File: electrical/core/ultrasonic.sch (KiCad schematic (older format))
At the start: 7 parts

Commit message: Annotation
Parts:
- gave numbers to parts that had none: 7

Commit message: Updated ultrassonic level shifter
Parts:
- removed Q3, Q4: 2N3904, Package_TO_SOT_THT:TO-92_Inline, symbol Transistor_BJT:2N3904
- removed R73: 2.2k, symbol Device:R
- added Q2, Q3: AO3400, Package_TO_SOT_SMD:SOT-23, symbol rasbot:AO3400
- added R70: 10k, symbol Device:R
- R71: value 2.2k -> 10k
- renumbered J6 to J5, R70 to R68, R72 to R69
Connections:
- net labels added: Power-
- net labels removed: GND
- wire segments 19 -> 20
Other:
- moved on the sheet: R68, R69

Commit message: Several updates. Can't remember them all
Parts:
- R100: renamed from R69; footprint (none) -> Resistor_SMD:R_0603_1608Metric
- R101: renamed from R70; footprint (none) -> Resistor_SMD:R_0603_1608Metric
- R102: renamed from R71; footprint (none) -> Resistor_SMD:R_0603_1608Metric
- R99: renamed from R68; footprint (none) -> Resistor_SMD:R_0603_1608Metric
- renumbered J5 to J10, Q2 to Q6, Q3 to Q7

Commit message: lots of changes
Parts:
- renumbered J10 to J9, R99 to R101, R100 to R102, R101 to R103, R102 to R104

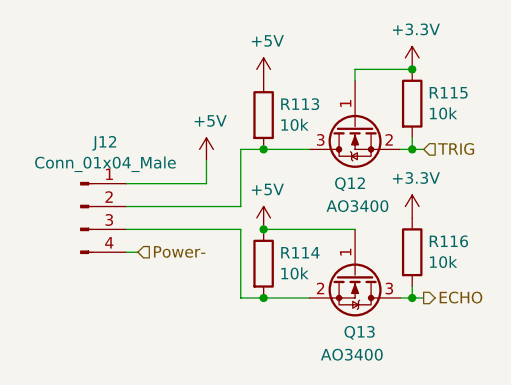
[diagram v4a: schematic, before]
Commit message: Reannotated after LDO romval
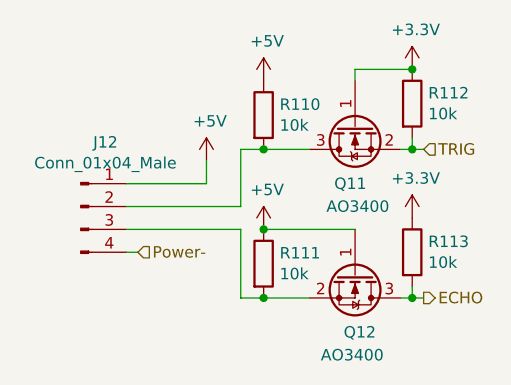
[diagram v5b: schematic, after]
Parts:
- renumbered Q6 to Q5, Q7 to Q6, R103 to R100, R104 to R101, R101 to R98, R102 to R99

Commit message: Re-annotated Schematic
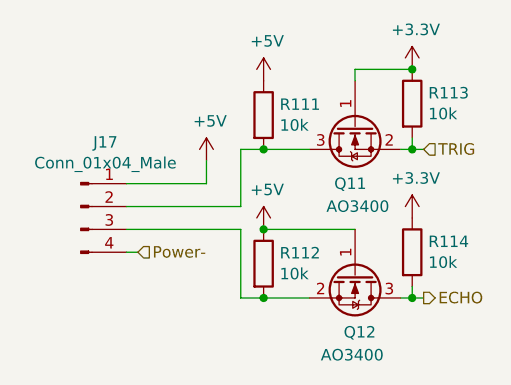
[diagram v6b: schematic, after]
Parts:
- renumbered J9 to J14, R99 to R100, R100 to R101, R101 to R102, R98 to R99
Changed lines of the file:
@@
 P 4650 3750
 AR Path="/5D1373A3/5DB4719C" Ref="J?"  Part="1"
-AR Path="/5D1373A3/5DB42710/5DB4719C" Ref="J9"  Part="1"
+AR Path="/5D1373A3/5DB42710/5DB4719C" Ref="J14"  Part="1"
 AR Path="/5D1373A3/5DBA0DBB/5DB4719C" Ref="J?"  Part="1"
 AR Path="/5D1373A3/5DBA1C1E/5DB4719C" Ref="J?"  Part="1"
@@
 AR Path="/5D1373A3/5DBA7DAA/5DB4719C" Ref="J?"  Part="1"
 AR Path="/5D1373A3/5DBA7DAF/5DB4719C" Ref="J?"  Part="1"
-AR Path="/5D1373A3/5E6481EF/5DB4719C" Ref="J10"  Part="1"
-AR Path="/5D1373A3/5E650C4B/5DB4719C" Ref="J11"  Part="1"
-AR Path="/5D1373A3/5E652B60/5DB4719C" Ref="J12"  Part="1"
-F 0 "J12" H 4758 4031 50  0000 C CNN
+AR Path="/5D1373A3/5E6481EF/5DB4719C" Ref="J15"  Part="1"
+AR Path="/5D1373A3/5E650C4B/5DB4719C" Ref="J16"  Part="1"
+AR Path="/5D1373A3/5E652B60/5DB4719C" Ref="J17"  Part="1"
+F 0 "J17" H 4758 4031 50  0000 C CNN
 F 1 "Conn_01x04_Male" H 4758 3940 50  0000 C CNN
 F 2 "Connector_PinHeader_2.54mm:PinHeader_1x04_P2.54mm_Vertical" H 4650 3750 50  0001 C CNN
@@
 P 5200 3550
 AR Path="/5D1373A3/5DB471A5" Ref="#PWR?"  Part="1"
-AR Path="/5D1373A3/5DB42710/5DB471A5" Ref="#PWR0279"  Part="1"
+AR Path="/5D1373A3/5DB42710/5DB471A5" Ref="#PWR0305"  Part="1"
 AR Path="/5D1373A3/5DBA0DBB/5DB471A5" Ref="#PWR?"  Part="1"
 AR Path="/5D1373A3/5DBA1C1E/5DB471A5" Ref="#PWR?"  Part="1"
@@
 AR Path="/5D1373A3/5DBA7DAA/5DB471A5" Ref="#PWR?"  Part="1"
 AR Path="/5D1373A3/5DBA7DAF/5DB471A5" Ref="#PWR?"  Part="1"
-AR Path="/5D1373A3/5E6481EF/5DB471A5" Ref="#PWR0284"  Part="1"
-AR Path="/5D1373A3/5E650C4B/5DB471A5" Ref="#PWR0289"  Part="1"
-AR Path="/5D1373A3/5E652B60/5DB471A5" Ref="#PWR0294"  Part="1"
-F 0 "#PWR0294" H 5200 3400 50  0001 C CNN
+AR Path="/5D1373A3/5E6481EF/5DB471A5" Ref="#PWR0310"  Part="1"
+AR Path="/5D1373A3/5E650C4B/5DB471A5" Ref="#PWR0315"  Part="1"
+AR Path="/5D1373A3/5E652B60/5DB471A5" Ref="#PWR0320"  Part="1"
+F 0 "#PWR0320" H 5200 3400 50  0001 C CNN
 F 1 "+5V" H 5215 3723 50  0000 C CNN
 F 2 "" H 5200 3550 50  0001 C CNN
@@
 TRIG
 $Comp
-L power:+5V #PWR0280
+L power:+5V #PWR0306
 U 1 1 5DB5AAB6
 P 5450 3200
-AR Path="/5D1373A3/5DB42710/5DB5AAB6" Ref="#PWR0280"  Part="1"
+AR Path="/5D1373A3/5DB42710/5DB5AAB6" Ref="#PWR0306"  Part="1"
 AR Path="/5D1373A3/5DBA0DBB/5DB5AAB6" Ref="#PWR?"  Part="1"
 AR Path="/5D1373A3/5DBA1C1E/5DB5AAB6" Ref="#PWR?"  Part="1"
@@
 AR Path="/5D1373A3/5DBA7DAA/5DB5AAB6" Ref="#PWR?"  Part="1"
 AR Path="/5D1373A3/5DBA7DAF/5DB5AAB6" Ref="#PWR?"  Part="1"
-AR Path="/5D1373A3/5E6481EF/5DB5AAB6" Ref="#PWR0285"  Part="1"
-AR Path="/5D1373A3/5E650C4B/5DB5AAB6" Ref="#PWR0290"  Part="1"
-AR Path="/5D1373A3/5E652B60/5DB5AAB6" Ref="#PWR0295"  Part="1"
-F 0 "#PWR0295" H 5450 3050 50  0001 C CNN
+AR Path="/5D1373A3/5E6481EF/5DB5AAB6" Ref="#PWR0311"  Part="1"
+AR Path="/5D1373A3/5E650C4B/5DB5AAB6" Ref="#PWR0316"  Part="1"
+AR Path="/5D1373A3/5E652B60/5DB5AAB6" Ref="#PWR0321"  Part="1"
+F 0 "#PWR0321" H 5450 3050 50  0001 C CNN
 F 1 "+5V" H 5465 3373 50  0000 C CNN
 F 2 "" H 5450 3200 50  0001 C CNN
@@
 ECHO
 $Comp
-L power:+3.3V #PWR0282
+L power:+3.3V #PWR0308
 U 1 1 5DB62EEB
 P 6100 3150
-AR Path="/5D1373A3/5DB42710/5DB62EEB" Ref="#PWR0282"  Part="1"
+AR Path="/5D1373A3/5DB42710/5DB62EEB" Ref="#PWR0308"  Part="1"
 AR Path="/5D1373A3/5DBA0DBB/5DB62EEB" Ref="#PWR?"  Part="1"
 AR Path="/5D1373A3/5DBA1C1E/5DB62EEB" Ref="#PWR?"  Part="1"
@@
 AR Path="/5D1373A3/5DBA7DAA/5DB62EEB" Ref="#PWR?"  Part="1"
 AR Path="/5D1373A3/5DBA7DAF/5DB62EEB" Ref="#PWR?"  Part="1"
-AR Path="/5D1373A3/5E6481EF/5DB62EEB" Ref="#PWR0287"  Part="1"
-AR Path="/5D1373A3/5E650C4B/5DB62EEB" Ref="#PWR0292"  Part="1"
-AR Path="/5D1373A3/5E652B60/5DB62EEB" Ref="#PWR0297"  Part="1"
-F 0 "#PWR0297" H 6100 3000 50  0001 C CNN
+AR Path="/5D1373A3/5E6481EF/5DB62EEB" Ref="#PWR0313"  Part="1"
+AR Path="/5D1373A3/5E650C4B/5DB62EEB" Ref="#PWR0318"  Part="1"
+AR Path="/5D1373A3/5E652B60/5DB62EEB" Ref="#PWR0323"  Part="1"
+F 0 "#PWR0323" H 6100 3000 50  0001 C CNN
 F 1 "+3.3V" H 6115 3323 50  0000 C CNN
 F 2 "" H 6100 3150 50  0001 C CNN
@@
 $EndComp
 $Comp
-L Device:R R99
+L Device:R R100
 U 1 1 5DB63B36
 P 5450 4000
-AR Path="/5D1373A3/5DB42710/5DB63B36" Ref="R99"  Part="1"
+AR Path="/5D1373A3/5DB42710/5DB63B36" Ref="R100"  Part="1"
 AR Path="/5D1373A3/5DBA0DBB/5DB63B36" Ref="R?"  Part="1"
 AR Path="/5D1373A3/5DBA1C1E/5DB63B36" Ref="R?"  Part="1"
@@
 AR Path="/5D1373A3/5DBA7DAA/5DB63B36" Ref="R?"  Part="1"
 AR Path="/5D1373A3/5DBA7DAF/5DB63B36" Ref="R?"  Part="1"
-AR Path="/5D1373A3/5E6481EF/5DB63B36" Ref="R103"  Part="1"
-AR Path="/5D1373A3/5E650C4B/5DB63B36" Ref="R107"  Part="1"
-AR Path="/5D1373A3/5E652B60/5DB63B36" Ref="R111"  Part="1"
-F 0 "R111" H 5520 4046 50  0000 L CNN
+AR Path="/5D1373A3/5E6481EF/5DB63B36" Ref="R104"  Part="1"
+AR Path="/5D1373A3/5E650C4B/5DB63B36" Ref="R108"  Part="1"
+AR Path="/5D1373A3/5E652B60/5DB63B36" Ref="R112"  Part="1"
+F 0 "R112" H 5520 4046 50  0000 L CNN
 F 1 "10k" H 5520 3955 50  0000 L CNN
 F 2 "Resistor_SMD:R_0603_1608Metric" V 5380 4000 50  0001 C CNN
@@
 $EndComp
 $Comp
-L Device:R R98
+L Device:R R99
 U 1 1 5DB640C0
 P 5450 3350
-AR Path="/5D1373A3/5DB42710/5DB640C0" Ref="R98"  Part="1"
+AR Path="/5D1373A3/5DB42710/5DB640C0" Ref="R99"  Part="1"
 AR Path="/5D1373A3/5DBA0DBB/5DB640C0" Ref="R?"  Part="1"
 AR Path="/5D1373A3/5DBA1C1E/5DB640C0" Ref="R?"  Part="1"
@@
 AR Path="/5D1373A3/5DBA7DAA/5DB640C0" Ref="R?"  Part="1"
 AR Path="/5D1373A3/5DBA7DAF/5DB640C0" Ref="R?"  Part="1"
-AR Path="/5D1373A3/5E6481EF/5DB640C0" Ref="R102"  Part="1"
-AR Path="/5D1373A3/5E650C4B/5DB640C0" Ref="R106"  Part="1"
-AR Path="/5D1373A3/5E652B60/5DB640C0" Ref="R110"  Part="1"
-F 0 "R110" H 5520 3396 50  0000 L CNN
+AR Path="/5D1373A3/5E6481EF/5DB640C0" Ref="R103"  Part="1"
+AR Path="/5D1373A3/5E650C4B/5DB640C0" Ref="R107"  Part="1"
+AR Path="/5D1373A3/5E652B60/5DB640C0" Ref="R111"  Part="1"
+F 0 "R111" H 5520 3396 50  0000 L CNN
 F 1 "10k" H 5520 3305 50  0000 L CNN
 F 2 "Resistor_SMD:R_0603_1608Metric" V 5380 3350 50  0001 C CNN
@@
 	5450 3500 5650 3500
 $Comp
-L power:+5V #PWR0281
+L power:+5V #PWR0307
 U 1 1 5E680E9A
 P 5450 3850
-AR Path="/5D1373A3/5DB42710/5E680E9A" Ref="#PWR0281"  Part="1"
+AR Path="/5D1373A3/5DB42710/5E680E9A" Ref="#PWR0307"  Part="1"
 AR Path="/5D1373A3/5DBA0DBB/5E680E9A" Ref="#PWR?"  Part="1"
 AR Path="/5D1373A3/5DBA1C1E/5E680E9A" Ref="#PWR?"  Part="1"
@@
 AR Path="/5D1373A3/5DBA7DAA/5E680E9A" Ref="#PWR?"  Part="1"
 AR Path="/5D1373A3/5DBA7DAF/5E680E9A" Ref="#PWR?"  Part="1"
-AR Path="/5D1373A3/5E6481EF/5E680E9A" Ref="#PWR0286"  Part="1"
-AR Path="/5D1373A3/5E650C4B/5E680E9A" Ref="#PWR0291"  Part="1"
-AR Path="/5D1373A3/5E652B60/5E680E9A" Ref="#PWR0296"  Part="1"
-F 0 "#PWR0296" H 5450 3700 50  0001 C CNN
+AR Path="/5D1373A3/5E6481EF/5E680E9A" Ref="#PWR0312"  Part="1"
+AR Path="/5D1373A3/5E650C4B/5E680E9A" Ref="#PWR0317"  Part="1"
+AR Path="/5D1373A3/5E652B60/5E680E9A" Ref="#PWR0322"  Part="1"
+F 0 "#PWR0322" H 5450 3700 50  0001 C CNN
 F 1 "+5V" H 5465 4023 50  0000 C CNN
 F 2 "" H 5450 3850 50  0001 C CNN
@@
 Connection ~ 5450 3850
 $Comp
-L Device:R R100
+L Device:R R101
 U 1 1 5E6822ED
 P 6100 3300
-AR Path="/5D1373A3/5DB42710/5E6822ED" Ref="R100"  Part="1"
+AR Path="/5D1373A3/5DB42710/5E6822ED" Ref="R101"  Part="1"
 AR Path="/5D1373A3/5DBA0DBB/5E6822ED" Ref="R?"  Part="1"
 AR Path="/5D1373A3/5DBA1C1E/5E6822ED" Ref="R?"  Part="1"
@@
 AR Path="/5D1373A3/5DBA7DAA/5E6822ED" Ref="R?"  Part="1"
 AR Path="/5D1373A3/5DBA7DAF/5E6822ED" Ref="R?"  Part="1"
-AR Path="/5D1373A3/5E6481EF/5E6822ED" Ref="R104"  Part="1"
-AR Path="/5D1373A3/5E650C4B/5E6822ED" Ref="R108"  Part="1"
-AR Path="/5D1373A3/5E652B60/5E6822ED" Ref="R112"  Part="1"
-F 0 "R112" H 6170 3346 50  0000 L CNN
+AR Path="/5D1373A3/5E6481EF/5E6822ED" Ref="R105"  Part="1"
+AR Path="/5D1373A3/5E650C4B/5E6822ED" Ref="R109"  Part="1"
+AR Path="/5D1373A3/5E652B60/5E6822ED" Ref="R113"  Part="1"
+F 0 "R113" H 6170 3346 50  0000 L CNN
 F 1 "10k" H 6170 3255 50  0000 L CNN
 F 2 "Resistor_SMD:R_0603_1608Metric" V 6030 3300 50  0001 C CNN
@@
 Connection ~ 6100 3500
 $Comp
-L Device:R R101
+L Device:R R102
 U 1 1 5E6835CA
 P 6100 3950
-AR Path="/5D1373A3/5DB42710/5E6835CA" Ref="R101"  Part="1"
+AR Path="/5D1373A3/5DB42710/5E6835CA" Ref="R102"  Part="1"
 AR Path="/5D1373A3/5DBA0DBB/5E6835CA" Ref="R?"  Part="1"
 AR Path="/5D1373A3/5DBA1C1E/5E6835CA" Ref="R?"  Part="1"
@@
 AR Path="/5D1373A3/5DBA7DAA/5E6835CA" Ref="R?"  Part="1"
 AR Path="/5D1373A3/5DBA7DAF/5E6835CA" Ref="R?"  Part="1"
-AR Path="/5D1373A3/5E6481EF/5E6835CA" Ref="R105"  Part="1"
-AR Path="/5D1373A3/5E650C4B/5E6835CA" Ref="R109"  Part="1"
-AR Path="/5D1373A3/5E652B60/5E6835CA" Ref="R113"  Part="1"
-F 0 "R113" H 6170 3996 50  0000 L CNN
+AR Path="/5D1373A3/5E6481EF/5E6835CA" Ref="R106"  Part="1"
+AR Path="/5D1373A3/5E650C4B/5E6835CA" Ref="R110"  Part="1"
+AR Path="/5D1373A3/5E652B60/5E6835CA" Ref="R114"  Part="1"
+F 0 "R114" H 6170 3996 50  0000 L CNN
 F 1 "10k" H 6170 3905 50  0000 L CNN
 F 2 "Resistor_SMD:R_0603_1608Metric" V 6030 3950 50  0001 C CNN
@@
 $EndComp
 $Comp
-L power:+3.3V #PWR0283
+L power:+3.3V #PWR0309
 U 1 1 5E68391F
 P 6100 3800
-AR Path="/5D1373A3/5DB42710/5E68391F" Ref="#PWR0283"  Part="1"
+AR Path="/5D1373A3/5DB42710/5E68391F" Ref="#PWR0309"  Part="1"
 AR Path="/5D1373A3/5DBA0DBB/5E68391F" Ref="#PWR?"  Part="1"
 AR Path="/5D1373A3/5DBA1C1E/5E68391F" Ref="#PWR?"  Part="1"
@@
 AR Path="/5D1373A3/5DBA7DAA/5E68391F" Ref="#PWR?"  Part="1"
 AR Path="/5D1373A3/5DBA7DAF/5E68391F" Ref="#PWR?"  Part="1"
-AR Path="/5D1373A3/5E6481EF/5E68391F" Ref="#PWR0288"  Part="1"
-AR Path="/5D1373A3/5E650C4B/5E68391F" Ref="#PWR0293"  Part="1"
-AR Path="/5D1373A3/5E652B60/5E68391F" Ref="#PWR0298"  Part="1"
-F 0 "#PWR0298" H 6100 3650 50  0001 C CNN
+AR Path="/5D1373A3/5E6481EF/5E68391F" Ref="#PWR0314"  Part="1"
+AR Path="/5D1373A3/5E650C4B/5E68391F" Ref="#PWR0319"  Part="1"
+AR Path="/5D1373A3/5E652B60/5E68391F" Ref="#PWR0324"  Part="1"
+F 0 "#PWR0324" H 6100 3650 50  0001 C CNN
 F 1 "+3.3V" H 6115 3973 50  0000 C CNN
 F 2 "" H 6100 3800 50  0001 C CNN

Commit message: Move IR board to different project
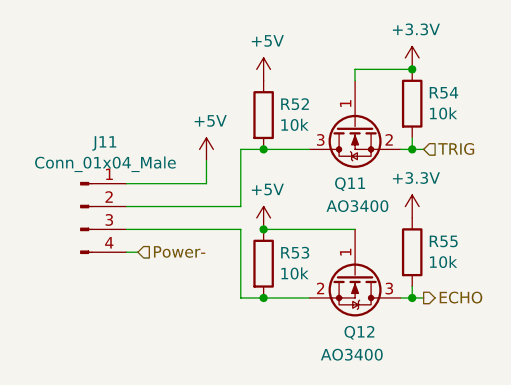
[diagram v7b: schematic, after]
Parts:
- renumbered J14 to J8, R99 to R40, R100 to R41, R101 to R42, R102 to R43
